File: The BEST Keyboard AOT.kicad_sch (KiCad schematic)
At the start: 5 parts, among them J1 Conn_01x02, Q1 FS8205A_C2830320, U1 DW01A, U2 TP4056_C382139

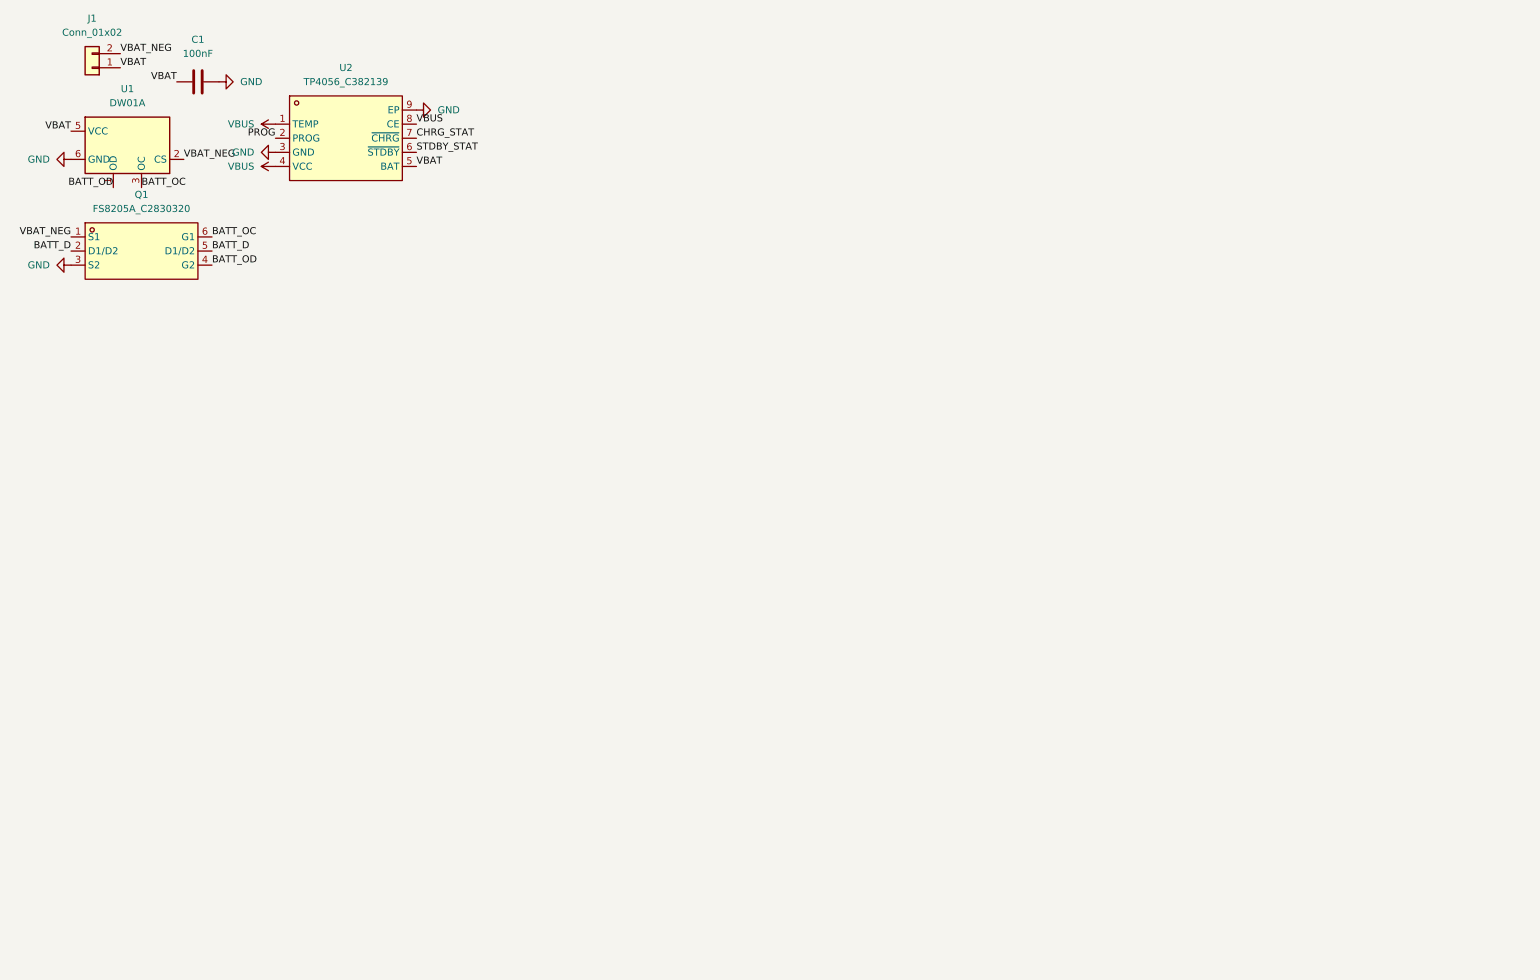
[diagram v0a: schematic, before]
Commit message: Update schematic and symbols
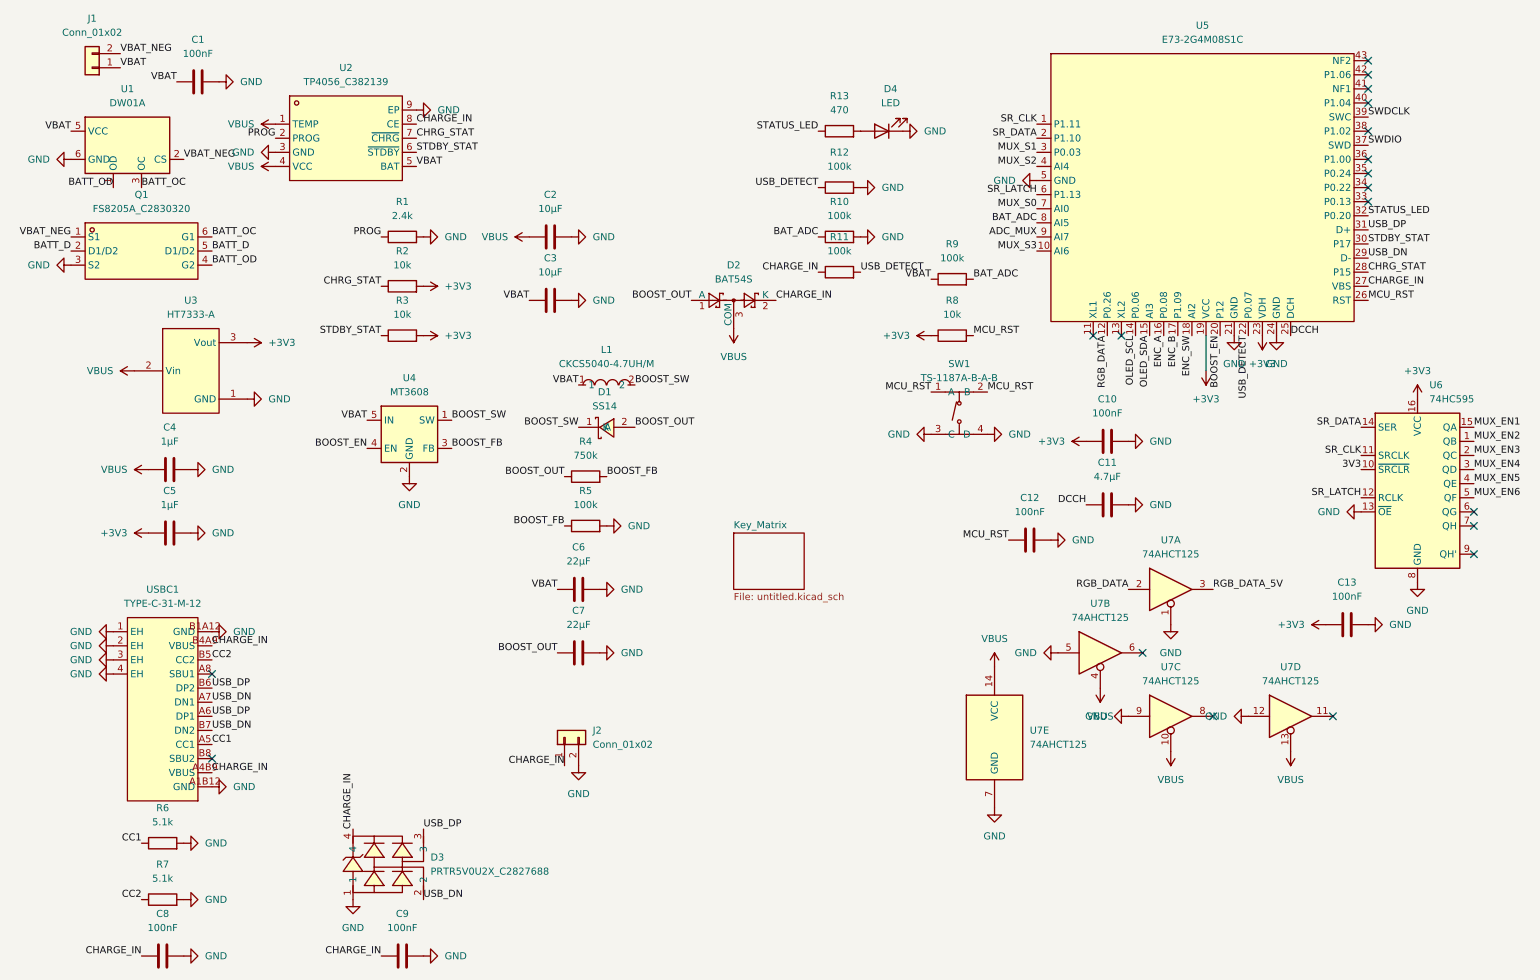
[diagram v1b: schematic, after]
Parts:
- added C10, C12, C13, C8, C9: 100nF, Capacitor_SMD:C_0402_1005Metric, symbol Device:C
- added C11: 4.7µF, Capacitor_SMD:C_0402_1005Metric, symbol Device:C
- added C2, C3: 10µF, Capacitor_SMD:C_0402_1005Metric, symbol Device:C
- added C4, C5: 1µF, Capacitor_SMD:C_0402_1005Metric, symbol Device:C
- added C6, C7: 22µF, Capacitor_SMD:C_0805_2012Metric, symbol Device:C
- added D1: SS14, keyboard:SMA_L4.2-W2.6-LS5.0-RD_1, symbol keyboard:SS14
- added D2: BAT54S, Package_TO_SOT_SMD:SOT-23, symbol Diode:BAT54S
- added D3: PRTR5V0U2X_C2827688, keyboard:SOT-143-4_L2.9-W1.3-P1.92-LS2.4-BL, symbol keyboard:PRTR5V0U2X_C2827688
- added D4: LED, LED_SMD:LED_0603_1608Metric, symbol Device:LED
- added J2: Conn_01x02, Connector_PinHeader_2.54mm:PinHeader_1x02_P2.54mm_Vertical, symbol Connector_Generic:Conn_01x02
- added L1: CKCS5040-4.7UH/M, keyboard:IND-SMD_L5.0-W5.0, symbol keyboard:CKCS5040-4.7UH_M
- added R1: 2.4k, Resistor_SMD:R_0402_1005Metric, symbol Device:R
- added R10, R11, R12, R5, R9: 100k, Resistor_SMD:R_0402_1005Metric, symbol Device:R
- added R13: 470, Resistor_SMD:R_0402_1005Metric, symbol Device:R
- added R2, R3, R8: 10k, Resistor_SMD:R_0402_1005Metric, symbol Device:R
- added R4: 750k, Resistor_SMD:R_0402_1005Metric, symbol Device:R
- added R6, R7: 5.1k, Resistor_SMD:R_0402_1005Metric, symbol Device:R
- added SW1: TS-1187A-B-A-B, keyboard:SW-SMD_4P-L5.1-W5.1-P3.70-LS6.5-TL_H1.5, symbol keyboard:TS-1187A-B-A-B
- added U3: HT7333-A, keyboard:SOT-89-3_L4.5-W2.5-P1.50-LS4.2-BR, symbol keyboard:HT7333-A
- added U4: MT3608, Package_TO_SOT_SMD:SOT-23-6, symbol Regulator_Switching:MT3608
- added U5: E73-2G4M08S1C, keyboard:WIRELM-SMD_E73-2G4M08S1C, symbol keyboard:E73-2G4M08S1C
- added U6: 74HC595, Package_SO:SOIC-16_3.9x9.9mm_P1.27mm, symbol 74xx:74HC595
- added U7: 74AHCT125, Package_SO:SOIC-14_3.9x8.7mm_P1.27mm, symbol 74xx:74AHCT125
- added USBC1: TYPE-C-31-M-12, keyboard:USB-C_SMD-TYPE-C-31-M-12_1, symbol keyboard:TYPE-C-31-M-12
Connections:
- net CHRG_STAT: now also R2.1, U5.28 (P15)
- net GND: now also C10.2, C11.2, C12.2, C13.2, C2.2, C3.2, C4.2, C5.2, C6.2, C7.2, C8.2, C9.2, D3.1, D4.1 (K), J2.2 (Pin_2), R1.2, R10.2, R12.2, R5.2, R6.2, R7.2, SW1.3 (C), SW1.4 (D), U3.1 (GND), U4.2 (GND), U5.21 (GND), U5.24 (GND), U5.5 (GND), U6.13 (~{OE}), U6.8 (GND), U7.1, U7.12, U7.5, U7.7 (GND), U7.9, USBC1.1 (EH), USBC1.2 (EH), USBC1.3 (EH), USBC1.4 (EH), USBC1.A1B12 (GND), USBC1.B1A12 (GND)
- net STDBY_STAT: now also R3.1, U5.30 (P17)
- net VBAT: now also C3.1, C6.1, L1.1, R9.1, U4.5 (IN)
- net VBUS: now also C2.1, C4.1, D2.3 (COM), U3.2 (Vin), U7.10, U7.13, U7.14 (VCC), U7.4; no longer U2.8 (CE)
- net at U2.2 (PROG): now also R1.1
- new net: D4.2 (A), R13.2
- new net +3V3: C10.1, C13.1, C5.1, R2.2, R3.2, R8.1, U3.3 (Vout), U5.19 (VCC), U5.23 (VDH), U6.16 (VCC)
- new net 3V3: U6.10 (~{SRCLR})
- new net ADC_MUX: U5.9 (AI7)
- new net BAT_ADC: R10.1, R9.2, U5.8 (AI5)
- new net BOOST_EN: U4.4 (EN), U5.20 (P12)
- new net BOOST_FB: R4.2, R5.1, U4.3 (FB)
- new net BOOST_OUT: C7.1, D1.2 (A), D2.1 (A), R4.1
- new net BOOST_SW: D1.1 (K), L1.2, U4.1 (SW)
- new net CC1: R6.1, USBC1.A5 (CC1)
- new net CC2: R7.1, USBC1.B5 (CC2)
- new net CHARGE_IN: C8.1, C9.1, D2.2 (K), D3.4, J2.1 (Pin_1), R11.1, U2.8 (CE), U5.27 (VBS), USBC1.A4B9 (VBUS), USBC1.B4A9 (VBUS)
- new net DCCH: C11.1, U5.25 (DCH)
- new net ENC_A: U5.16 (P0.08)
- new net ENC_B: U5.17 (P1.09)
- new net ENC_SW: U5.18 (AI2)
- new net MCU_RST: C12.1, R8.2, SW1.1 (A), SW1.2 (B), U5.26 (RST)
- new net MUX_EN1: U6.15 (QA)
- new net MUX_EN2: U6.1 (QB)
- new net MUX_EN3: U6.2 (QC)
- new net MUX_EN4: U6.3 (QD)
- new net MUX_EN5: U6.4 (QE)
- new net MUX_EN6: U6.5 (QF)
- new net MUX_S0: U5.7 (AI0)
- new net MUX_S1: U5.3 (P0.03)
- new net MUX_S2: U5.4 (AI4)
- new net MUX_S3: U5.10 (AI6)
- new net OLED_SCL: U5.14 (P0.06)
- new net OLED_SDA: U5.15 (AI3)
- new net RGB_DATA: U5.12 (P0.26), U7.2
- new net RGB_DATA_5V: U7.3
- new net SR_CLK: U5.1 (P1.11), U6.11 (SRCLK)
- new net SR_DATA: U5.2 (P1.10), U6.14 (SER)
- new net SR_LATCH: U5.6 (P1.13), U6.12 (RCLK)
- new net STATUS_LED: R13.1, U5.32 (P0.20)
- new net SWDCLK: U5.39 (SWC)
- new net SWDIO: U5.37 (SWD)
- new net USB_DETECT: R11.2, R12.1, U5.22 (P0.07)
- new net USB_DN: D3.2, U5.29 (D-), USBC1.A7 (DN1), USBC1.B7 (DN2)
- new net USB_DP: D3.3, U5.31 (D+), USBC1.A6 (DP1), USBC1.B6 (DP2)
- no-connect marks 0 -> 19
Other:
- added sheet Key_Matrix (untitled.kicad_sch)
